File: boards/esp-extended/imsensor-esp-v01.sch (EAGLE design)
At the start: 42 parts, among them J1-A2 PJ-313-SPAD, J2-A3 PJ-313-SPAD, J3-A4 PJ-313-SPAD, J4-A5 PJ-313-SPAD, J5-D9 PJ-313-SPAD, J6-D6 PJ-313-SPAD, J7-D5 PJ-313-SPAD, J8-D3 PJ-313-SPAD, Q1 MOSFET-NCHANNEL2N7000, Q2 MOSFET-NCHANNEL2N7000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

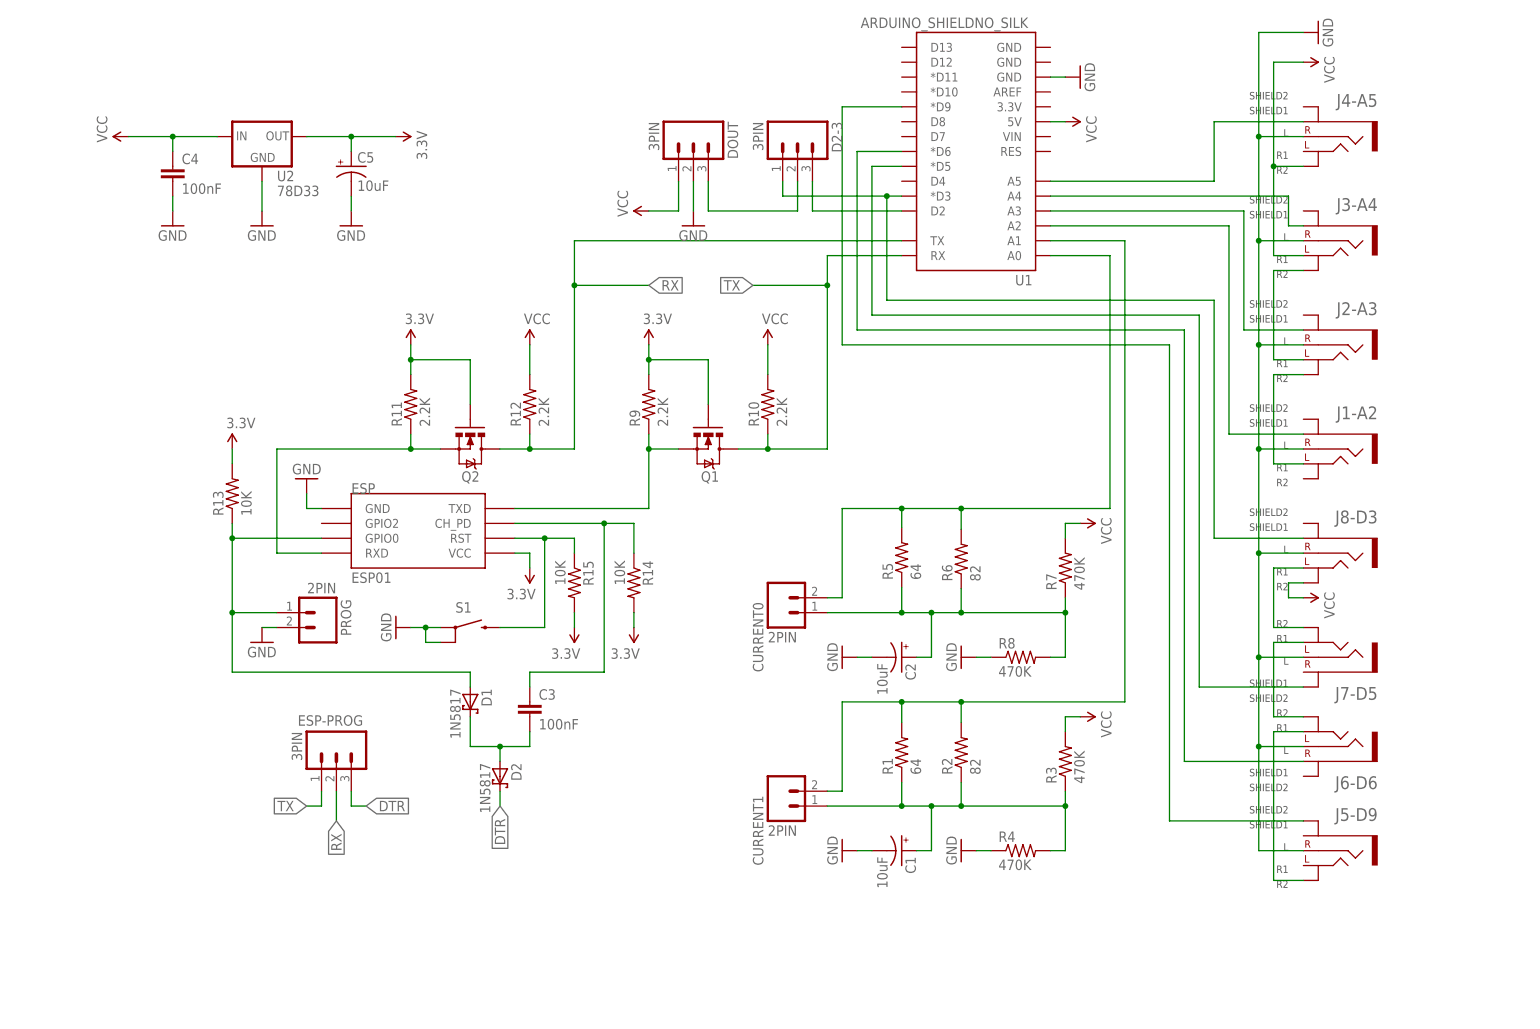
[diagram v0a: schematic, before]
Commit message: Cleaned and organized IMSensor for ESP8266 V1
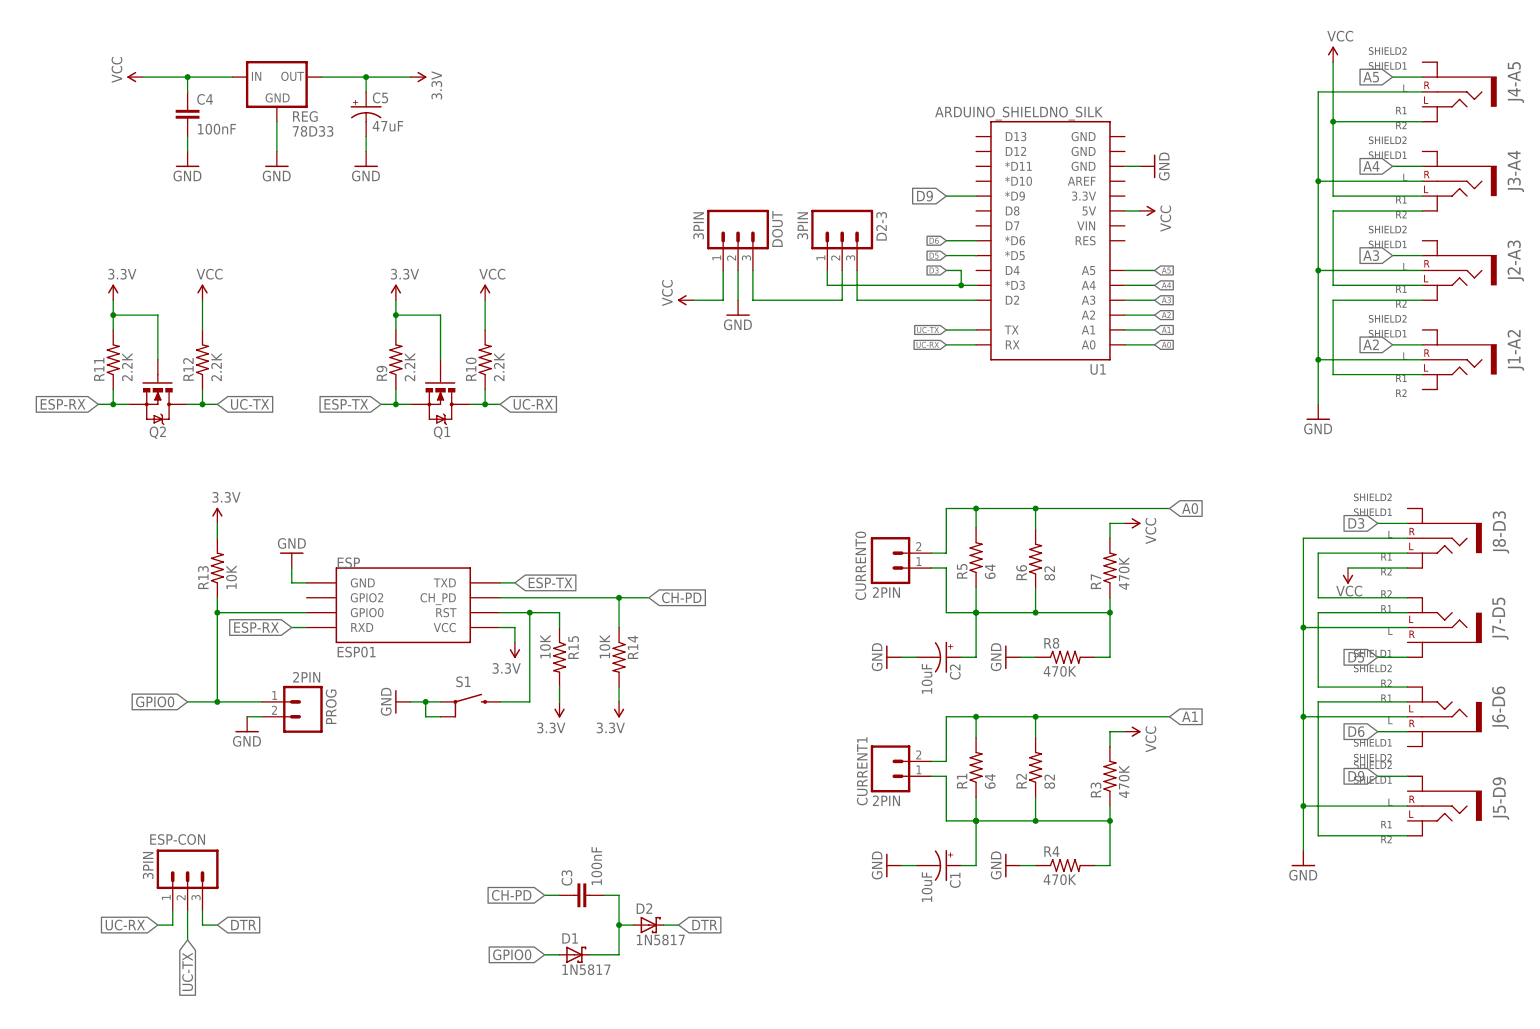
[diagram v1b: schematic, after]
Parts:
- removed ESP-PROG: 3PIN, SparkFun-Connectors:M03PTH
- removed U2: 78D33, salvador-parts-imported:V_REG_78XXSINK
- added ESP-CON: 3PIN, SparkFun-Connectors:M03PTH
- added REG: 78D33, salvador-parts-imported:V_REG_78XXSINK
- C5: value 10uF -> 47uF
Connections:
- net DEK renamed A0
- net J5 renamed D6
- net N$10 renamed A1
- net N$11 renamed BURDEN-C1
- net N$12 renamed D9
- net N$13 renamed D3
- net N$15 renamed A5
- net N$17 renamed BURDEN-C0
- net N$18 renamed ESP-TX
- net N$20 renamed RST
- net N$21 renamed ESP-RX
- net N$22 renamed CH-PD
- net N$25 renamed GPIO0
- net N$3 renamed A4
- net N$4 renamed A3
- net N$5 renamed A2
- net N$6 renamed D5
- removed net RX: ESP-PROG.2, Q2.D, R12.1, U1.TX
- removed net TX: ESP-PROG.1, Q1.D, R10.1, U1.RX
- new net UC-RX: ESP-CON.1, Q1.D, R10.1, U1.RX
- new net UC-TX: ESP-CON.2, Q2.D, R12.1, U1.TX
- net 3.3V: now also REG.OUT; no longer U2.OUT
- net DTR: now also ESP-CON.3; no longer ESP-PROG.3
- net GND: now also REG.GND; no longer U2.GND
- net VCC: now also REG.IN; no longer U2.IN
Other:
- note added: "3.3V POWER SUPPLY"
- note added: "5V - 3.3V BIDIRECTIONAL UART CONVERTER"
- note added: "ESP8266"
- note added: "ESP8266 CONNECTOR"
- note added: "ESP8266 FTDI-AUTORESET"
- note added: "IMWiserNode - ARDUINO SHIELD Version 0.1"
- moved on the sheet: C1, C2, C3, C4, C5, CURRENT0, CURRENT1, D1, D2, D2-3, DOUT, ESP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
